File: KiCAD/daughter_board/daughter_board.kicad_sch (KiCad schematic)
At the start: 7 parts, among them U1 TPS61023DRLR

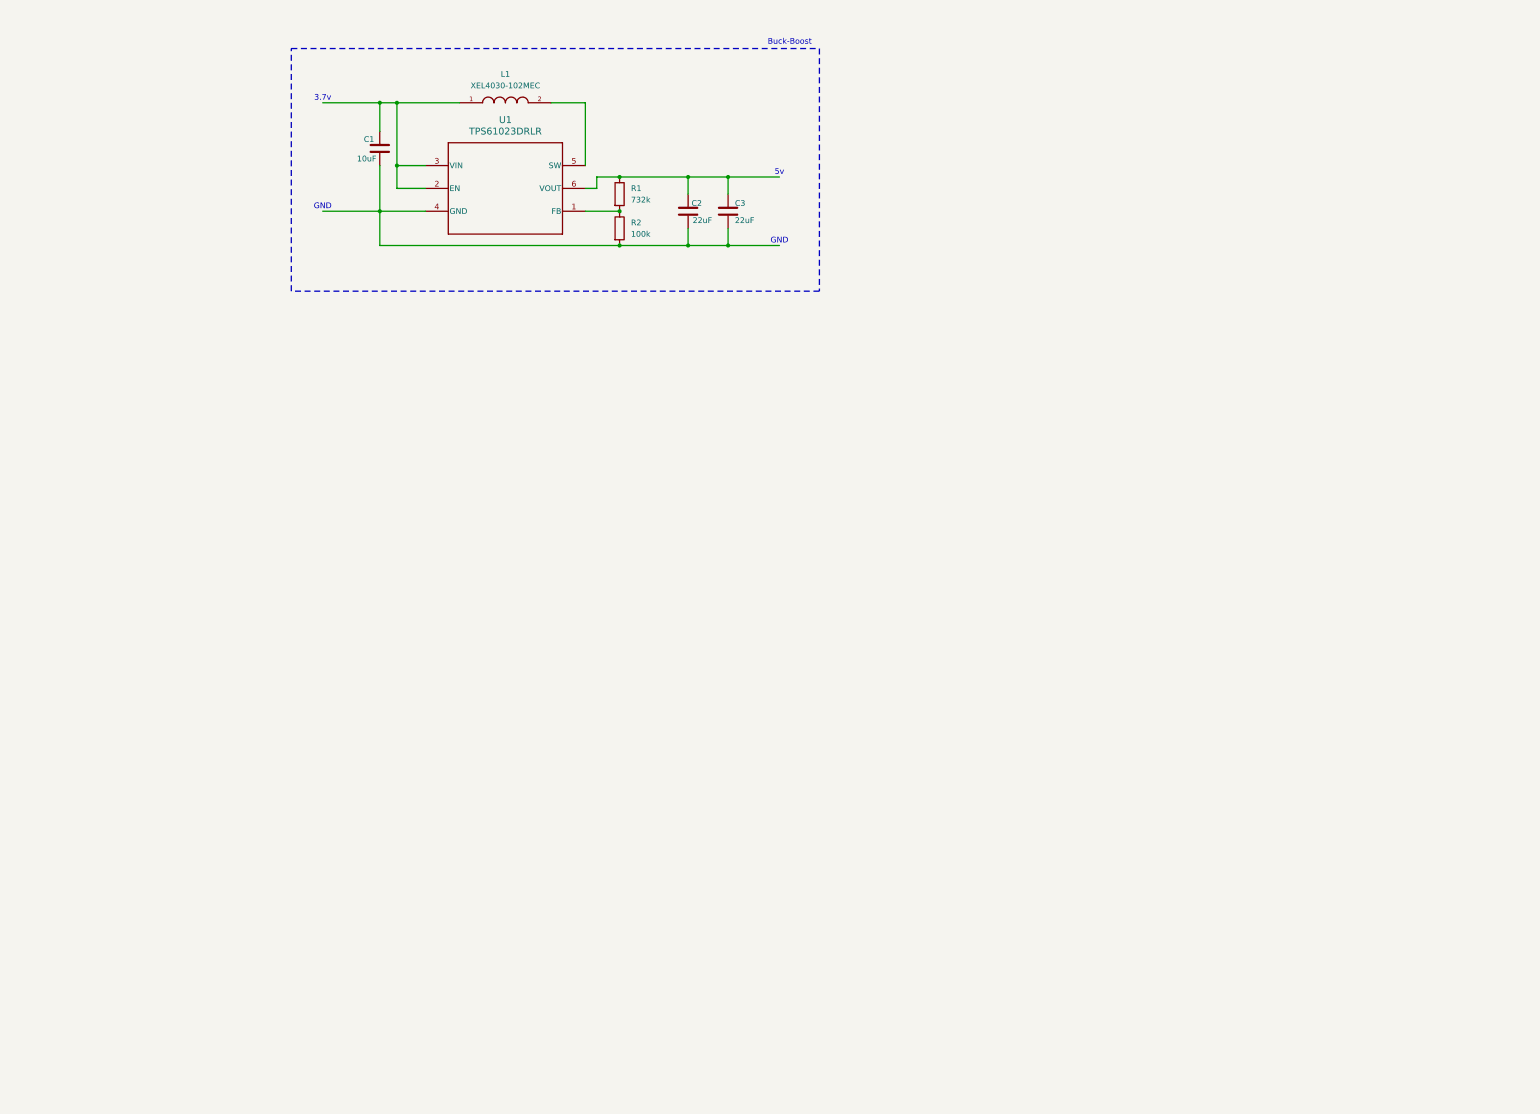
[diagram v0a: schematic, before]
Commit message: in /Kicad/daughterboard added the mpu6050 schematic in the daughter board
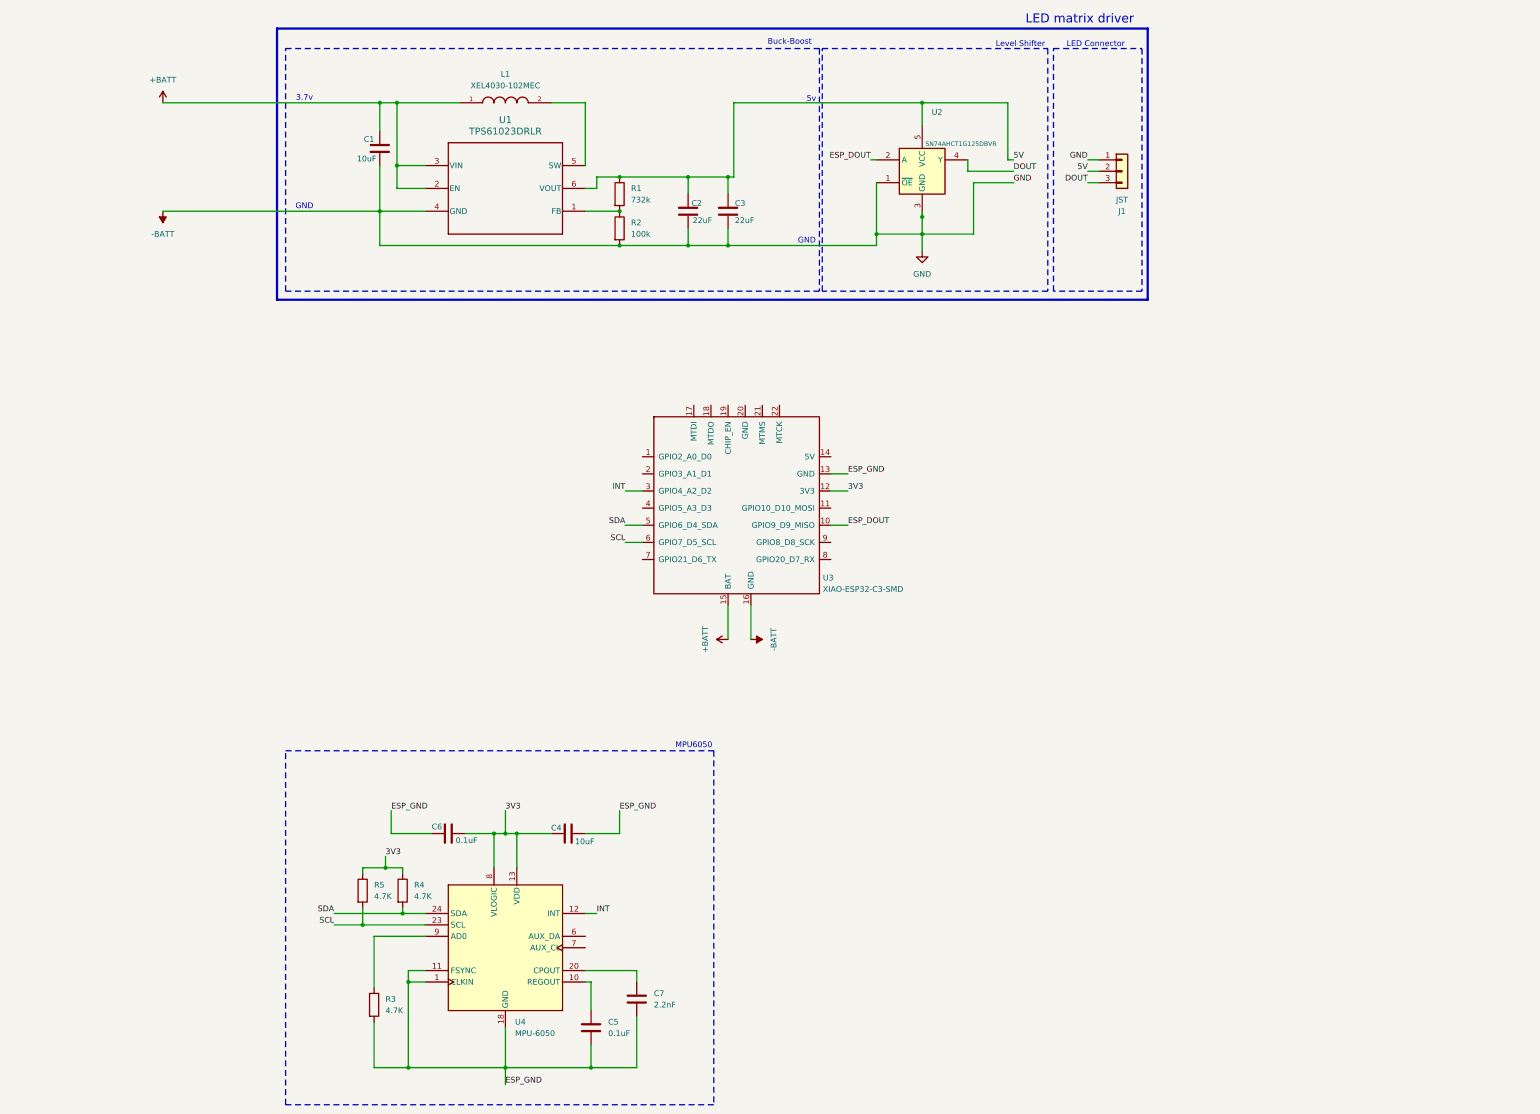
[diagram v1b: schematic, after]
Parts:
- added C4: 10uF, Capacitor_SMD:C_0603_1608Metric_Pad1.08x0.95mm_HandSolder, symbol Device:C
- added C5, C6: 0.1uF, Capacitor_SMD:C_0603_1608Metric_Pad1.08x0.95mm_HandSolder, symbol Device:C
- added C7: 2.2nF, Capacitor_SMD:C_0603_1608Metric_Pad1.08x0.95mm_HandSolder, symbol Device:C
- added J1: JST, Connector_JST:JST_SH_SM03B-SRSS-TB_1x03-1MP_P1.00mm_Horizontal, symbol Connector_Generic:Conn_01x03
- added R3, R4, R5: 4.7K, Resistor_SMD:R_0603_1608Metric_Pad0.98x0.95mm_HandSolder, symbol Device:R
- added U2: SN74AHCT1G125DBVR, Package_TO_SOT_SMD:SOT-23-5, symbol 74xGxx:NC7SZ125M5X
- added U3: XIAO-ESP32-C3-SMD, My_Custom_Footprints:XIAO-ESP32C3-SMD, symbol Seeed_Studio_XIAO_Series:XIAO-ESP32-C3-SMD
- added U4: MPU-6050, Sensor_Motion:InvenSense_QFN-24_4x4mm_P0.5mm_NoMask, symbol Sensor_Motion:MPU-6050
- C1, C2, C3: footprint Capacitor_SMD:C_0805_2012Metric_Pad1.18x1.45mm_HandSolder -> Capacitor_SMD:C_0603_1608Metric_Pad1.08x0.95mm_HandSolder
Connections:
- net 5V: now reaches C2.1, C3.1, R1.1, U1.6 (VOUT)
- net 5V: now also J1.2 (Pin_2), U2.5 (VCC)
- net -BATT: now reaches C1.2, C2.2, C3.2, R2.2, U1.4 (GND)
- net -BATT: now also J1.1 (Pin_1), U2.1 (~{OE}), U2.3 (GND), U3.16 (GND)
- net +BATT: now reaches C1.1, L1.1, U1.2 (EN), U1.3 (VIN)
- net +BATT: now also U3.15 (BAT)
- new net: C5.1, U4.10 (REGOUT)
- new net: C7.1, U4.20 (CPOUT)
- new net: R3.1, U4.9 (AD0)
- new net 3V3: C4.2, C6.1, R4.1, R5.1, U3.12 (3V3), U4.13 (VDD), U4.8 (VLOGIC)
- new net DOUT: J1.3 (Pin_3), U2.4 (Y)
- new net ESP_DOUT: U2.2 (A), U3.10 (GPIO9_D9_MISO)
- new net ESP_GND: C4.1, C5.2, C6.2, C7.2, R3.2, U3.13 (GND), U4.1 (CLKIN), U4.11 (FSYNC), U4.18 (GND)
- new net INT: U3.3 (GPIO4_A2_D2), U4.12 (INT)
- new net SCL: R5.2, U3.6 (GPIO7_D5_SCL), U4.23 (SCL)
- new net SDA: R4.2, U3.5 (GPIO6_D4_SDA), U4.24 (SDA)
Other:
- note added: "LED Connector"
- note added: "LED matrix driver"
- note added: "Level Shifter"
- note added: "MPU6050"

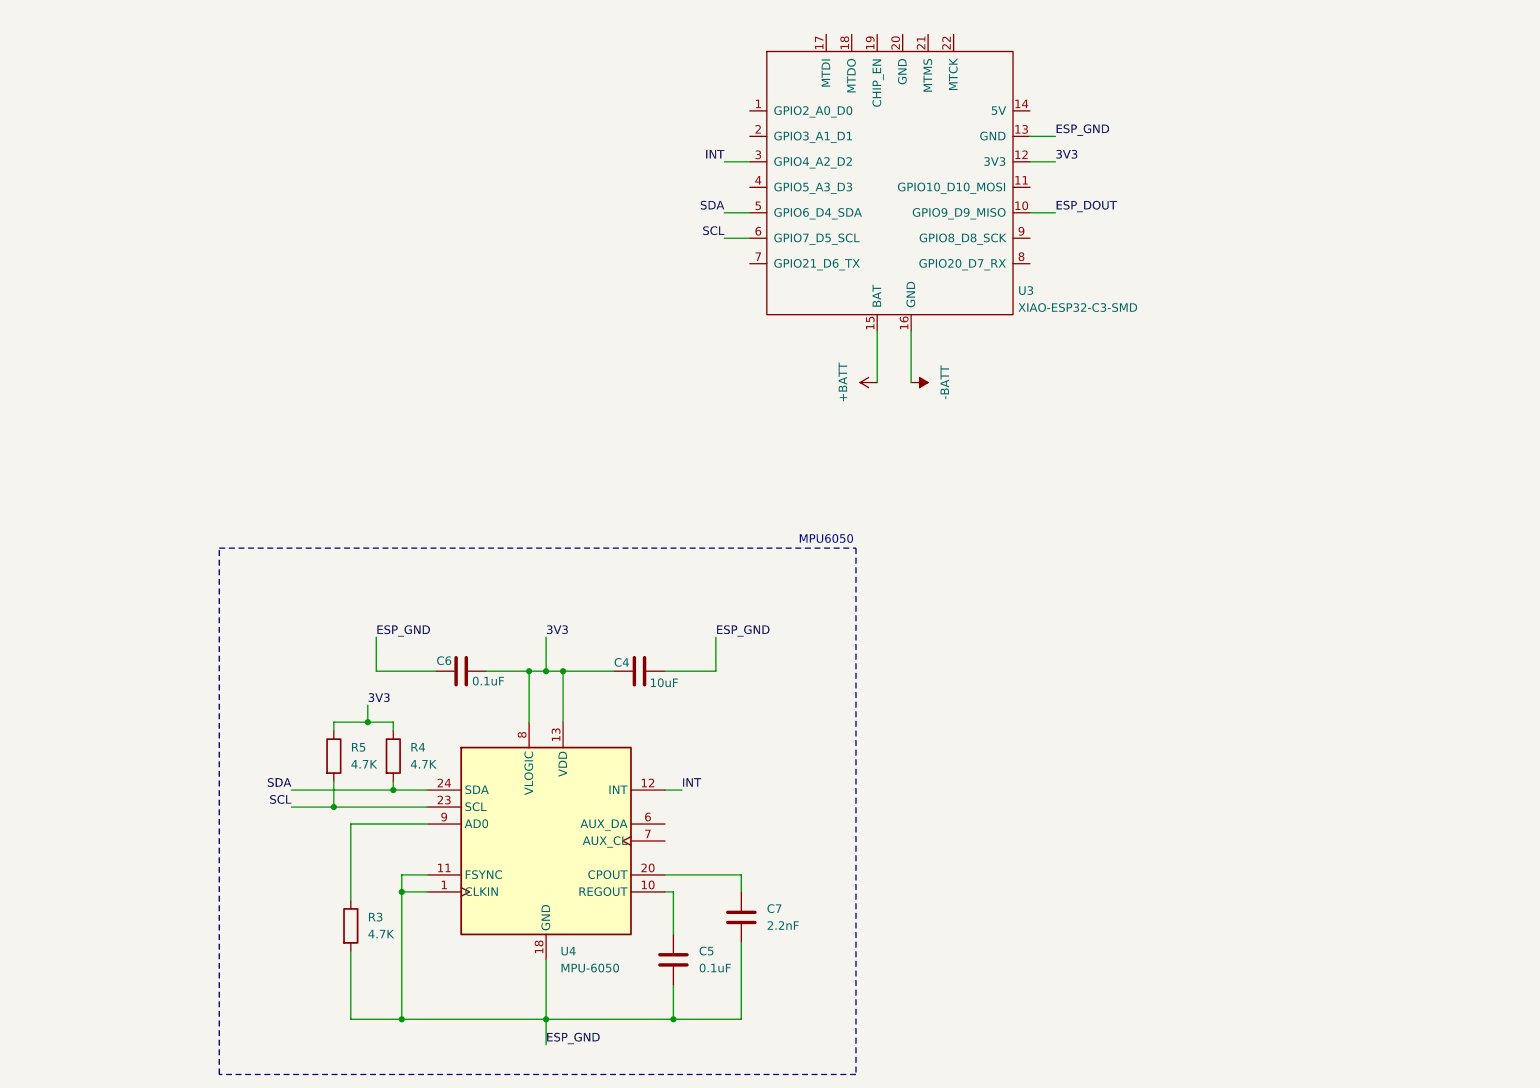
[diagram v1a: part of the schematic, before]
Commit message: added datasheets, 3d models and alsocreated the schematic for qmc5883L
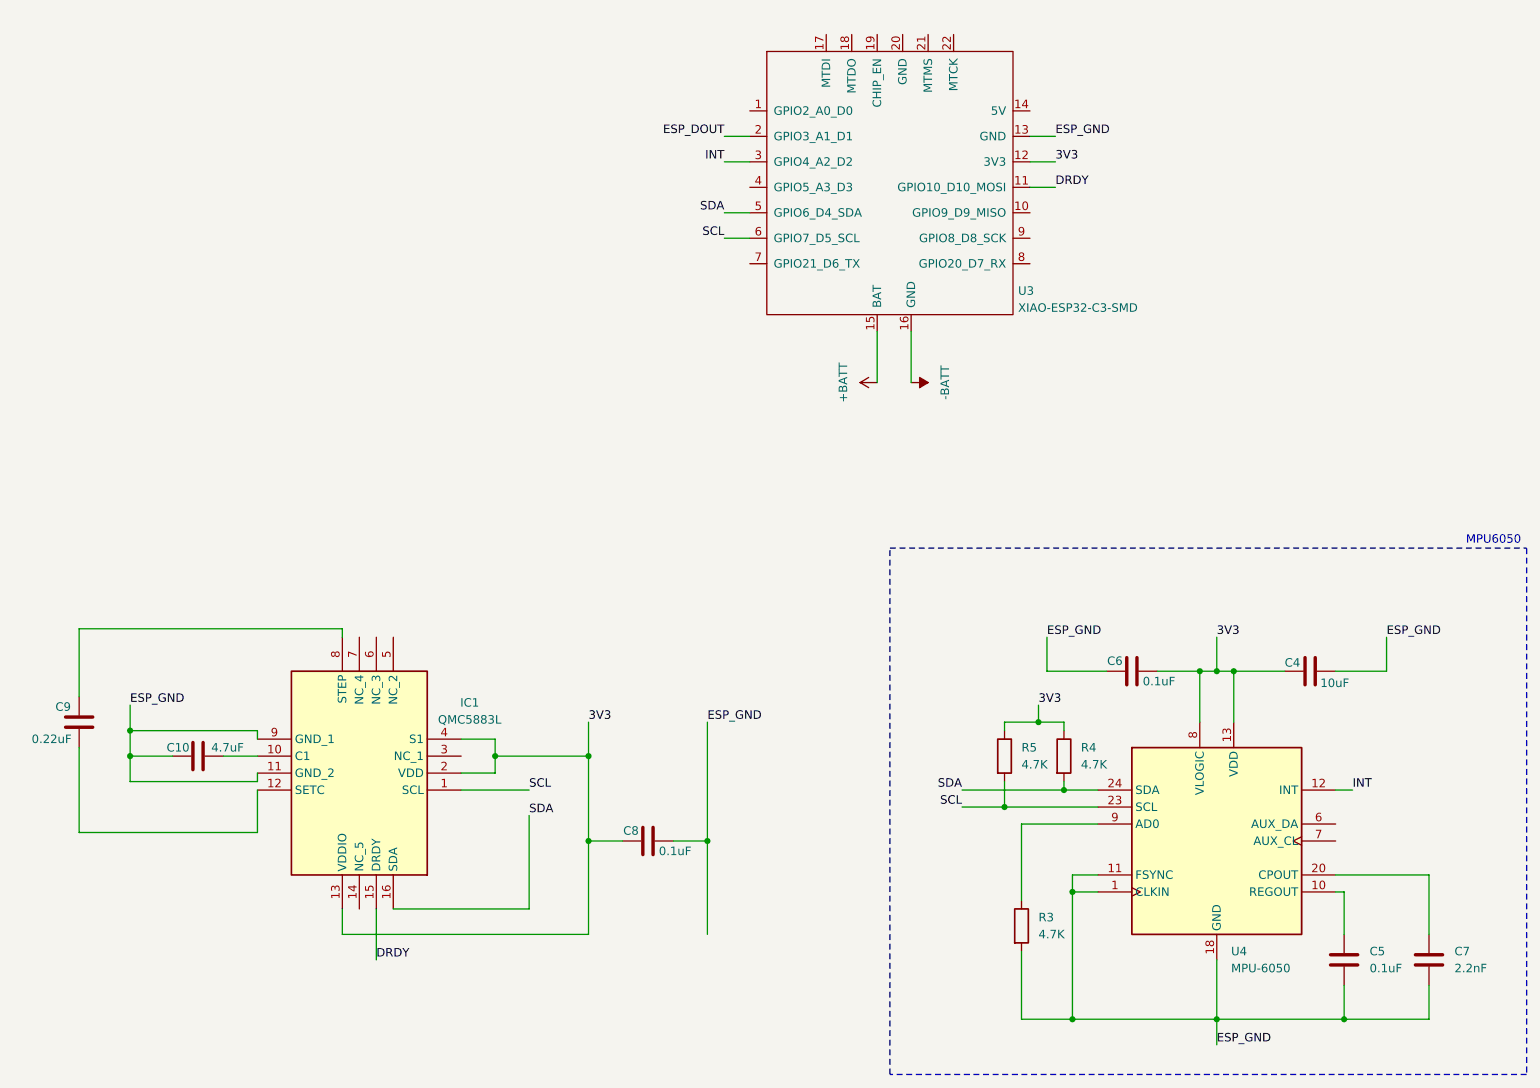
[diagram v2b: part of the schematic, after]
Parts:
- added C10: 4.7uF, Capacitor_SMD:C_0603_1608Metric_Pad1.08x0.95mm_HandSolder, symbol Device:C
- added C8: 0.1uF, Capacitor_SMD:C_0603_1608Metric_Pad1.08x0.95mm_HandSolder, symbol Device:C
- added C9: 0.22uF, Capacitor_SMD:C_0603_1608Metric_Pad1.08x0.95mm_HandSolder, symbol Device:C
- added IC1: QMC5883L, custom_lib:QMC5883L, symbol QMC5883L:QMC5883L
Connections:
- net 3V3: now also C8.2, IC1.13 (VDDIO), IC1.2 (VDD), IC1.4 (S1)
- net ESP_DOUT: now also U3.2 (GPIO3_A1_D1); no longer U3.10 (GPIO9_D9_MISO)
- net ESP_GND: now also C10.2, C8.1, IC1.11 (GND_2), IC1.9 (GND_1)
- net SCL: now also IC1.1 (SCL)
- net SDA: now also IC1.16 (SDA)
- net DRDY: now reaches U3.11 (GPIO10_D10_MOSI)
- net DRDY: now also IC1.15 (DRDY)
- new net: C10.1, IC1.10 (C1)
- new net: C9.1, IC1.12 (SETC)
- new net: C9.2, IC1.8 (STEP)
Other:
- moved on the sheet: C4, C5, C6, C7, R3, R4, R5, U4
